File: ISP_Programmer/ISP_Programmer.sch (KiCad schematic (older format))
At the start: 19 parts, among them IC1 ATTINY2313-S, P1 CONN_02X03, P2 USB_OTG, P3 CONN_02X03, U2 74LS125, X1 CRYSTAL_SMD

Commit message: checking
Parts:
- P2: footprint Connect:USB_Micro-B -> DM_Custom:DM_USB_MICRO
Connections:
- net GND: now also D2.1 (K); no longer R7.2
- net at IC1.12 ((PCINT0/AIN0)PB0): now also R7.2; no longer D2.2 (A)
- net at R7.1: now also D2.2 (A); no longer D2.1 (K)
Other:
- moved on the sheet: D2, R7
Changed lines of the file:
@@
 F 0 "P2" H 6125 5575 50  0000 C CNN
 F 1 "USB_OTG" H 5800 5900 50  0000 C CNN
-F 2 "Connect:USB_Micro-B" V 5750 5600 50  0001 C CNN
+F 2 "DM_Custom:DM_USB_MICRO" V 5750 5600 50  0001 C CNN
 F 3 "" V 5750 5600 50  0000 C CNN
 	1    5800 5700
@@
 L LED D2
 U 1 1 592413A0
-P 4650 4600
-F 0 "D2" H 4650 4700 50  0000 C CNN
-F 1 "LED" H 4650 4500 50  0000 C CNN
-F 2 "LEDs:LED_0805" H 4650 4600 50  0001 C CNN
-F 3 "" H 4650 4600 50  0000 C CNN
-	1    4650 4600
-	-1   0    0    1
+P 5000 4800
+F 0 "D2" H 5000 4900 50  0000 C CNN
+F 1 "LED" H 5000 4700 50  0000 C CNN
+F 2 "LEDs:LED_0805" H 5000 4800 50  0001 C CNN
+F 3 "" H 5000 4800 50  0000 C CNN
+	1    5000 4800
+	0    -1   -1   0
 $EndComp
 $Comp
@@
 L R R7
 U 1 1 592416F7
-P 5000 4850
-F 0 "R7" V 5080 4850 50  0000 C CNN
-F 1 "1K" V 5000 4850 50  0000 C CNN
-F 2 "Resistors_SMD:R_0603_HandSoldering" V 4930 4850 50  0001 C CNN
-F 3 "" H 5000 4850 50  0000 C CNN
-	1    5000 4850
-	1    0    0    -1
+P 4650 4600
+F 0 "R7" V 4730 4600 50  0000 C CNN
+F 1 "1K" V 4650 4600 50  0000 C CNN
+F 2 "Resistors_SMD:R_0603_HandSoldering" V 4580 4600 50  0001 C CNN
+F 3 "" H 4650 4600 50  0000 C CNN
+	1    4650 4600
+	0    1    1    0
 $EndComp
 $Comp
@@
 $EndComp
 Wire Wire Line
-	4050 4600 4450 4600
-Wire Wire Line
-	4850 4600 5000 4600
-Wire Wire Line
-	5000 4600 5000 4700
+	4050 4600 4500 4600
 Wire Wire Line
 	5000 5100 5000 5000
@@
 Text Label 6450 3850 0    60   ~ 0
 GND
+Wire Wire Line
+	4800 4600 5000 4600
 $EndSCHEMATC

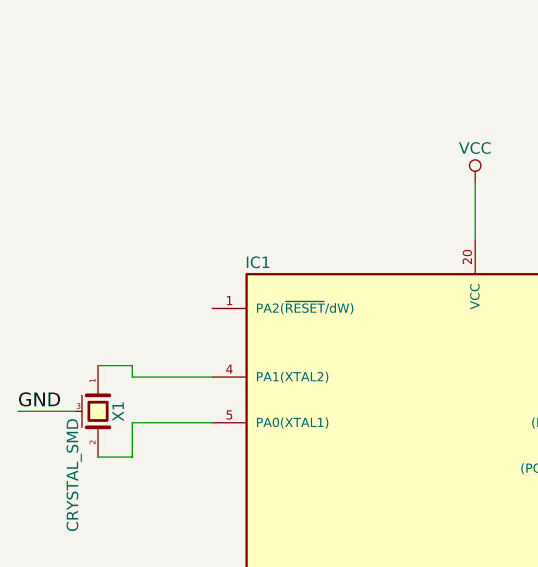
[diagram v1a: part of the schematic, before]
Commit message: added ISP programmer reset pull up
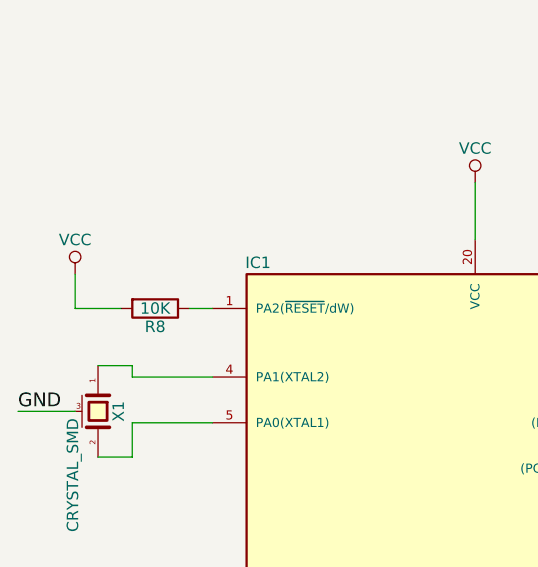
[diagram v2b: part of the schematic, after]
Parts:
- added R8: 10K, Resistors_SMD:R_0603_HandSoldering, symbol R
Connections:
- net VCC: now also R8.2
- net at IC1.1 (PA2(~RESET~/dW)): now also R8.1
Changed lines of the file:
@@
 Wire Wire Line
 	4800 4600 5000 4600
+$Comp
+L R R8
+U 1 1 59363E66
+P 1500 4600
+F 0 "R8" V 1580 4600 50  0000 C CNN
+F 1 "10K" V 1500 4600 50  0000 C CNN
+F 2 "Resistors_SMD:R_0603_HandSoldering" V 1430 4600 50  0001 C CNN
+F 3 "" H 1500 4600 50  0000 C CNN
+	1    1500 4600
+	0    1    1    0
+$EndComp
+$Comp
+L VCC #PWR012
+U 1 1 59363EF1
+P 1150 4450
+F 0 "#PWR012" H 1150 4300 50  0001 C CNN
+F 1 "VCC" H 1150 4600 50  0000 C CNN
+F 2 "" H 1150 4450 50  0000 C CNN
+F 3 "" H 1150 4450 50  0000 C CNN
+	1    1150 4450
+	1    0    0    -1
+$EndComp
+Wire Wire Line
+	1150 4600 1150 4450
+Wire Wire Line
+	1150 4600 1350 4600
+Wire Wire Line
+	1650 4600 1750 4600
 $EndSCHEMATC
